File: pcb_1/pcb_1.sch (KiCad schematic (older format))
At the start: 46 parts, among them J1 ACin, J2 Vout, J3 2N3055_conn, J4 DCin, P1 CONN_01X07, P2 CONN_01X01, P3 CONN_01X01, P4 CONN_01X01, P5 CONN_01X01, P6 CONN_01X01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

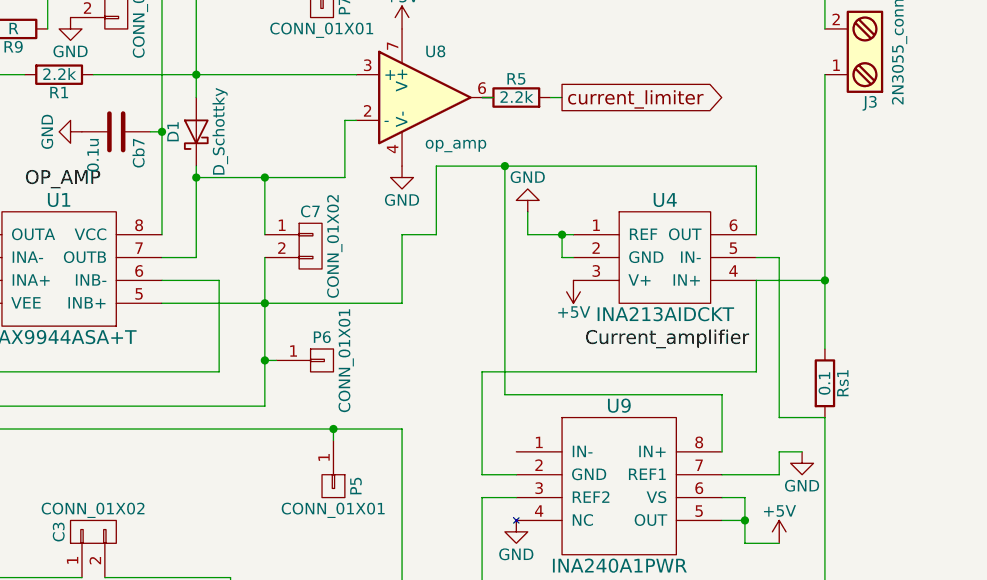
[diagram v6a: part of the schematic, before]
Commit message: INA240 kotelo vaihdettu ja toinen vastaava vahvistin poistettu
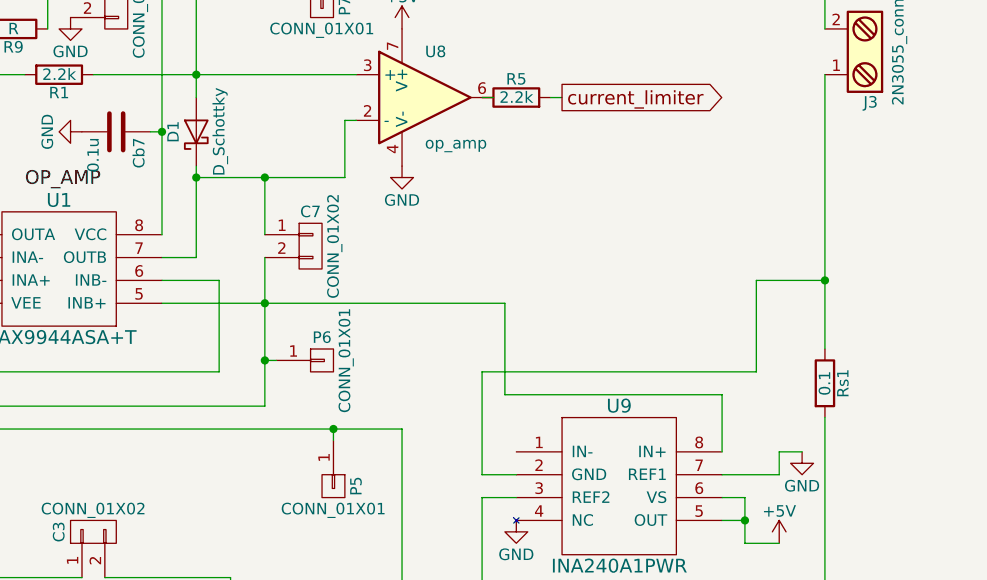
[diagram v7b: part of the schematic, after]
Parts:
- removed U4: INA213AIDCKT, TO_SOT_Packages_SMD:SOT-363_SC-70-6_Handsoldering, symbol INA213AIDCKT
- U9: footprint Housings_SSOP:TSSOP-8_4.4x3mm_Pitch0.65mm -> Housings_SOIC:SOIC-8_3.9x4.9mm_Pitch1.27mm
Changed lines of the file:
@@
-$EndComp
-$Comp
-L INA213AIDCKT U4
-U 1 1 5DA96BAA
-P 9750 2600
-F 0 "U4" H 9750 2850 60  0000 C CNN
-F 1 "INA213AIDCKT" H 9750 2350 60  0000 C CNN
-F 2 "TO_SOT_Packages_SMD:SOT-363_SC-70-6_Handsoldering" H 9750 2550 60  0001 C CNN
-F 3 "" H 9750 2550 60  0001 C CNN
-	1    9750 2600
-	1    0    0    -1
 $EndComp
 $Comp
@@
 $Comp
 L GND #PWR05
-U 1 1 5DA99EAF
-P 9150 2400
-F 0 "#PWR05" H 9150 2150 50  0001 C CNN
-F 1 "GND" H 9150 2250 50  0000 C CNN
-F 2 "" H 9150 2400 50  0000 C CNN
-F 3 "" H 9150 2400 50  0000 C CNN
-	1    9150 2400
-	-1   0    0    1
-$EndComp
-$Comp
-L GND #PWR06
 U 1 1 5DA99EE1
 P 9400 5750
-F 0 "#PWR06" H 9400 5500 50  0001 C CNN
+F 0 "#PWR05" H 9400 5500 50  0001 C CNN
 F 1 "GND" H 9400 5600 50  0000 C CNN
 F 2 "" H 9400 5750 50  0000 C CNN
@@
 $EndComp
 $Comp
-L GND #PWR07
+L GND #PWR06
 U 1 1 5DA99F13
 P 5100 3700
-F 0 "#PWR07" H 5100 3450 50  0001 C CNN
+F 0 "#PWR06" H 5100 3450 50  0001 C CNN
 F 1 "GND" H 5100 3550 50  0000 C CNN
 F 2 "" H 5100 3700 50  0000 C CNN
@@
 $EndComp
 $Comp
-L GND #PWR08
+L GND #PWR07
 U 1 1 5DA99F45
 P 7850 5100
-F 0 "#PWR08" H 7850 4850 50  0001 C CNN
+F 0 "#PWR07" H 7850 4850 50  0001 C CNN
 F 1 "GND" H 7850 4950 50  0000 C CNN
 F 2 "" H 7850 5100 50  0000 C CNN
@@
 $EndComp
 $Comp
-L GND #PWR09
+L GND #PWR08
 U 1 1 5DA9A00F
 P 5900 2200
-F 0 "#PWR09" H 5900 1950 50  0001 C CNN
+F 0 "#PWR08" H 5900 1950 50  0001 C CNN
 F 1 "GND" H 5900 2050 50  0000 C CNN
 F 2 "" H 5900 2200 50  0000 C CNN
@@
 $EndComp
 $Comp
-L GND #PWR010
+L GND #PWR09
 U 1 1 5DA9A041
 P 4400 4250
-F 0 "#PWR010" H 4400 4000 50  0001 C CNN
+F 0 "#PWR09" H 4400 4000 50  0001 C CNN
 F 1 "GND" H 4400 4100 50  0000 C CNN
 F 2 "" H 4400 4250 50  0000 C CNN
@@
 $EndComp
 $Comp
-L GND #PWR011
+L GND #PWR010
 U 1 1 5DA9A073
 P 4400 4650
-F 0 "#PWR011" H 4400 4400 50  0001 C CNN
+F 0 "#PWR010" H 4400 4400 50  0001 C CNN
 F 1 "GND" H 4400 4500 50  0000 C CNN
 F 2 "" H 4400 4650 50  0000 C CNN
@@
 $EndComp
 $Comp
-L GND #PWR012
+L GND #PWR011
 U 1 1 5DA9A83E
 P 6400 4550
-F 0 "#PWR012" H 6400 4300 50  0001 C CNN
+F 0 "#PWR011" H 6400 4300 50  0001 C CNN
 F 1 "GND" H 6400 4400 50  0000 C CNN
 F 2 "" H 6400 4550 50  0000 C CNN
@@
 $EndComp
 $Comp
-L +5V #PWR013
+L +5V #PWR012
 U 1 1 5DA9AC10
 P 6800 4850
-F 0 "#PWR013" H 6800 4700 50  0001 C CNN
+F 0 "#PWR012" H 6800 4700 50  0001 C CNN
 F 1 "+5V" H 6800 4990 50  0000 C CNN
 F 2 "" H 6800 4850 50  0000 C CNN
@@
 Text Label 6950 2300 0    60   ~ 0
 OP_AMP
-Text Label 9400 3000 0    60   ~ 0
-Current_amplifier
 Text Label 7000 5200 0    60   ~ 0
 Charge_pump
@@
 ADC_sda
 $Comp
-L GND #PWR014
+L GND #PWR013
 U 1 1 5DA9DC7C
 P 4550 1300
-F 0 "#PWR014" H 4550 1050 50  0001 C CNN
+F 0 "#PWR013" H 4550 1050 50  0001 C CNN
 F 1 "GND" H 4550 1150 50  0000 C CNN
 F 2 "" H 4550 1300 50  0000 C CNN
@@
 $EndComp
 $Comp
-L GND #PWR015
+L GND #PWR014
 U 1 1 5DA9E862
 P 6450 1600
-F 0 "#PWR015" H 6450 1350 50  0001 C CNN
+F 0 "#PWR014" H 6450 1350 50  0001 C CNN
 F 1 "GND" H 6450 1450 50  0000 C CNN
 F 2 "" H 6450 1600 50  0000 C CNN
@@
 ADC_sda
 $Comp
-L GND #PWR016
+L GND #PWR015
 U 1 1 5DAA07BA
 P 1700 2600
-F 0 "#PWR016" H 1700 2350 50  0001 C CNN
+F 0 "#PWR015" H 1700 2350 50  0001 C CNN
 F 1 "GND" H 1700 2450 50  0000 C CNN
 F 2 "" H 1700 2600 50  0000 C CNN
@@
 $EndComp
 $Comp
-L +5V #PWR017
+L +5V #PWR016
 U 1 1 5DAA1D85
 P 8600 1600
-F 0 "#PWR017" H 8600 1450 50  0001 C CNN
+F 0 "#PWR016" H 8600 1450 50  0001 C CNN
 F 1 "+5V" H 8600 1740 50  0000 C CNN
 F 2 "" H 8600 1600 50  0000 C CNN
@@
 $EndComp
 $Comp
-L GND #PWR018
+L GND #PWR017
 U 1 1 5DAA1DC9
 P 8600 2200
-F 0 "#PWR018" H 8600 1950 50  0001 C CNN
+F 0 "#PWR017" H 8600 1950 50  0001 C CNN
 F 1 "GND" H 8600 2050 50  0000 C CNN
 F 2 "" H 8600 2200 50  0000 C CNN
@@
 $EndComp
 $Comp
-L GND #PWR019
+L GND #PWR018
 U 1 1 5DAA4E05
 P 3200 1200
-F 0 "#PWR019" H 3200 950 50  0001 C CNN
+F 0 "#PWR018" H 3200 950 50  0001 C CNN
 F 1 "GND" H 3200 1050 50  0000 C CNN
 F 2 "" H 3200 1200 50  0000 C CNN
@@
 $EndComp
 $Comp
-L GND #PWR020
+L GND #PWR019
 U 1 1 5DAA97B0
 P 8350 4550
-F 0 "#PWR020" H 8350 4300 50  0001 C CNN
+F 0 "#PWR019" H 8350 4300 50  0001 C CNN
 F 1 "GND" H 8350 4400 50  0000 C CNN
 F 2 "" H 8350 4550 50  0000 C CNN
@@
 $EndComp
 $Comp
-L GND #PWR021
+L GND #PWR020
 U 1 1 5DAAA1EB
 P 6150 2200
-F 0 "#PWR021" H 6150 1950 50  0001 C CNN
+F 0 "#PWR020" H 6150 1950 50  0001 C CNN
 F 1 "GND" H 6150 2050 50  0000 C CNN
 F 2 "" H 6150 2200 50  0000 C CNN
@@
 $EndComp
 $Comp
-L GND #PWR022
+L GND #PWR021
 U 1 1 5DAAA2C9
 P 7150 1550
-F 0 "#PWR022" H 7150 1300 50  0001 C CNN
+F 0 "#PWR021" H 7150 1300 50  0001 C CNN
 F 1 "GND" H 7150 1400 50  0000 C CNN
 F 2 "" H 7150 1550 50  0000 C CNN
@@
 $EndComp
 $Comp
-L GND #PWR023
+L GND #PWR022
 U 1 1 5DAAC6FE
 P 3700 3150
-F 0 "#PWR023" H 3700 2900 50  0001 C CNN
+F 0 "#PWR022" H 3700 2900 50  0001 C CNN
 F 1 "GND" H 3700 3000 50  0000 C CNN
 F 2 "" H 3700 3150 50  0000 C CNN
@@
 $EndComp
 $Comp
-L GND #PWR024
+L GND #PWR023
 U 1 1 5DAAC74C
 P 3200 3000
-F 0 "#PWR024" H 3200 2750 50  0001 C CNN
+F 0 "#PWR023" H 3200 2750 50  0001 C CNN
 F 1 "GND" H 3200 2850 50  0000 C CNN
 F 2 "" H 3200 3000 50  0000 C CNN
@@
 $EndComp
 $Comp
-L GND #PWR025
+L GND #PWR024
 U 1 1 5DAADEFA
 P 5950 1100
-F 0 "#PWR025" H 5950 850 50  0001 C CNN
+F 0 "#PWR024" H 5950 850 50  0001 C CNN
 F 1 "GND" H 5950 950 50  0000 C CNN
 F 2 "" H 5950 1100 50  0000 C CNN
@@
 	1    5950 1100
 	0    -1   -1   0
-$EndComp
-$Comp
-L +5V #PWR026
-U 1 1 5DAB2129
-P 9350 2700
-F 0 "#PWR026" H 9350 2550 50  0001 C CNN
-F 1 "+5V" H 9350 2840 50  0000 C CNN
-F 2 "" H 9350 2700 50  0000 C CNN
-F 3 "" H 9350 2700 50  0000 C CNN
-	1    9350 2700
-	-1   0    0    1
 $EndComp
 $Comp
@@
 $EndComp
 $Comp
-L GND #PWR027
+L GND #PWR025
 U 1 1 5DAB514F
 P 4800 2450
-F 0 "#PWR027" H 4800 2200 50  0001 C CNN
+F 0 "#PWR025" H 4800 2200 50  0001 C CNN
 F 1 "GND" H 4800 2300 50  0000 C CNN
 F 2 "" H 4800 2450 50  0000 C CNN
@@
 $EndComp
 $Comp
-L GND #PWR028
+L GND #PWR026
 U 1 1 5DAB07B7
 P 7200 2050
-F 0 "#PWR028" H 7200 1800 50  0001 C CNN
+F 0 "#PWR026" H 7200 1800 50  0001 C CNN
 F 1 "GND" H 7200 1900 50  0000 C CNN
 F 2 "" H 7200 2050 50  0000 C CNN
@@
 F 0 "U9" H 9550 3950 60  0000 C CNN
 F 1 "INA240A1PWR" H 9550 3250 60  0000 C CNN
-F 2 "Housings_SSOP:TSSOP-8_4.4x3mm_Pitch0.65mm" H 9550 3250 60  0001 C CNN
+F 2 "Housings_SOIC:SOIC-8_3.9x4.9mm_Pitch1.27mm" H 9550 3250 60  0001 C CNN
 F 3 "" H 9550 3250 60  0001 C CNN
 	1    9550 3600
@@
 $EndComp
 $Comp
-L GND #PWR029
+L GND #PWR027
 U 1 1 5DAB6D92
 P 9100 3750
-F 0 "#PWR029" H 9100 3500 50  0001 C CNN
+F 0 "#PWR027" H 9100 3500 50  0001 C CNN
 F 1 "GND" H 9100 3600 50  0000 C CNN
 F 2 "" H 9100 3750 50  0000 C CNN
@@
 $EndComp
 $Comp
-L GND #PWR030
+L GND #PWR028
 U 1 1 5DAB710F
 P 10350 3450
-F 0 "#PWR030" H 10350 3200 50  0001 C CNN
+F 0 "#PWR028" H 10350 3200 50  0001 C CNN
 F 1 "GND" H 10350 3300 50  0000 C CNN
 F 2 "" H 10350 3450 50  0000 C CNN
@@
 $EndComp
 $Comp
-L +5V #PWR031
+L +5V #PWR029
 U 1 1 5DAB72B5
 P 10250 3850
-F 0 "#PWR031" H 10250 3700 50  0001 C CNN
+F 0 "#PWR029" H 10250 3700 50  0001 C CNN
 F 1 "+5V" H 10250 3990 50  0000 C CNN
 F 2 "" H 10250 3850 50  0000 C CNN
@@
 $EndComp
 $Comp
-L GND #PWR032
+L GND #PWR030
 U 1 1 5DABB706
 P 2200 1300
-F 0 "#PWR032" H 2200 1050 50  0001 C CNN
+F 0 "#PWR030" H 2200 1050 50  0001 C CNN
 F 1 "GND" H 2200 1150 50  0000 C CNN
 F 2 "" H 2200 1300 50  0000 C CNN
@@
 $EndComp
 $Comp
-L GND #PWR033
+L GND #PWR031
 U 1 1 5DABD497
 P 1700 1100
-F 0 "#PWR033" H 1700 850 50  0001 C CNN
+F 0 "#PWR031" H 1700 850 50  0001 C CNN
 F 1 "GND" H 1700 950 50  0000 C CNN
 F 2 "" H 1700 1100 50  0000 C CNN
@@
 	7800 2700 7550 2700
 Wire Wire Line
-	10450 3300 10250 3300
-Wire Wire Line
-	10250 3300 10250 2600
-Wire Wire Line
-	10250 2600 10150 2600
-Wire Wire Line
 	10450 1800 10450 3000
 Wire Wire Line
-	10150 2200 10150 2500
-Wire Wire Line
-	7550 2800 8600 2800
+	7550 2800 9050 2800
 Wire Wire Line
 	5350 900  5350 1250
@@
 Wire Wire Line
 	6300 1850 6150 1850
-Wire Wire Line
-	9150 2500 9350 2500
-Wire Wire Line
-	9150 2500 9150 2400
 Wire Wire Line
 	4650 1950 4800 1950
@@
 	6200 2600 6650 2600
 Connection ~ 9400 4950
-Wire Wire Line
-	9350 2600 9300 2600
-Wire Wire Line
-	9300 2600 9300 2500
-Connection ~ 9300 2500
 Wire Wire Line
 	9400 5350 9400 5750
@@
 Connection ~ 8300 4950
 Wire Wire Line
-	8750 2200 10150 2200
-Wire Wire Line
 	10150 2700 10450 2700
 Connection ~ 10450 2700
@@
 	10000 3200 9050 3200
 Wire Wire Line
-	9050 3200 9050 2200
-Connection ~ 9050 2200
-Wire Wire Line
 	8250 1300 8250 1250
 Connection ~ 8250 1250
@@
 Wire Wire Line
 	8000 2600 8000 3250
-Wire Wire Line
-	8600 2800 8600 2500
-Wire Wire Line
-	8600 2500 8750 2500
 Wire Wire Line
 	6350 2950 6350 2700
@@
 	6750 1600 6750 1500
 Wire Wire Line
-	8750 2500 8750 2200
+	9050 3200 9050 2800
 $EndSCHEMATC

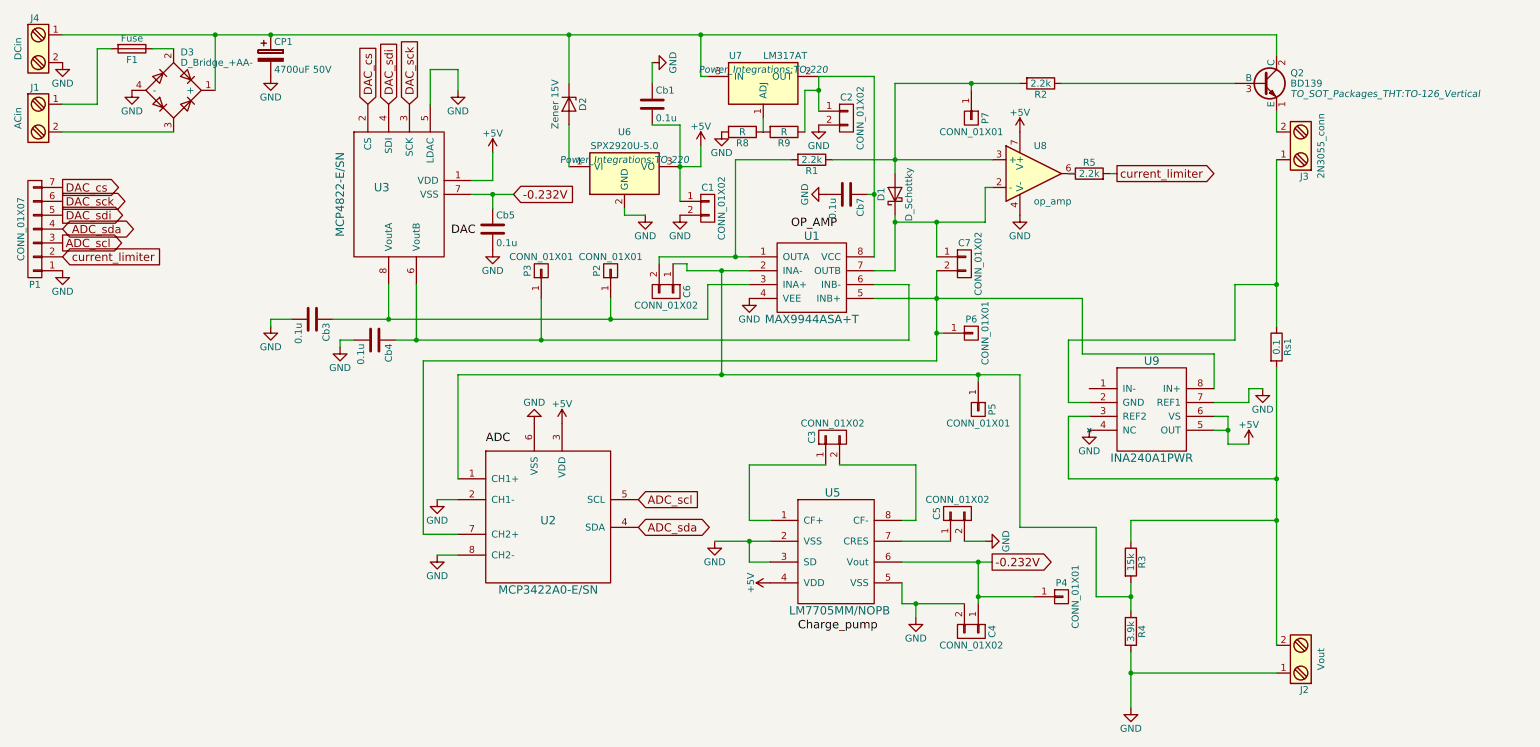
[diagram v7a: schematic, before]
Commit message: pcb:ssa nyt smd- ja tht-komponentit eri puolilla
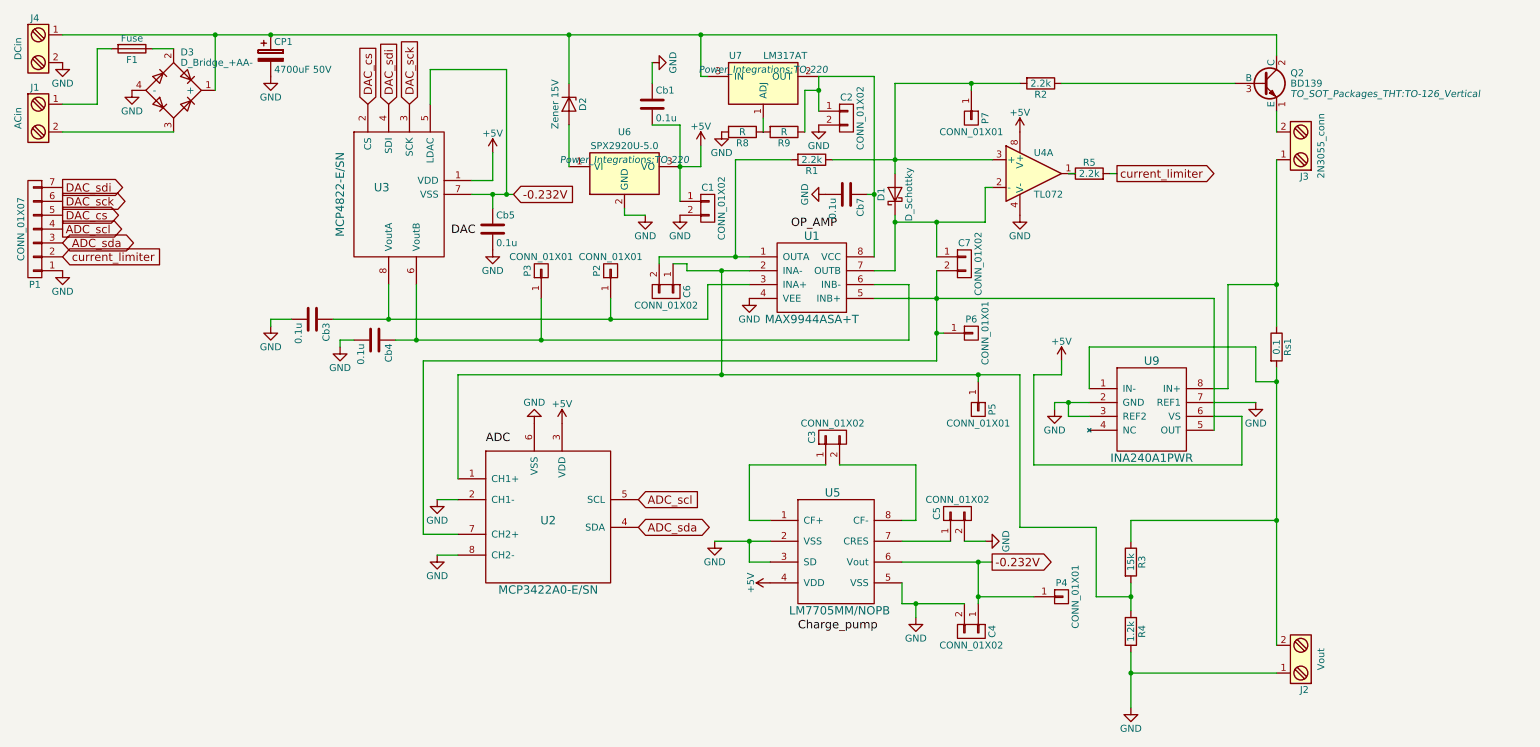
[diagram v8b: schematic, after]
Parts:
- removed U8: op_amp, Housings_SSOP:TSSOP-8_3x3mm_Pitch0.65mm, symbol TL081
- added U4: TL072, Housings_DIP:DIP-8_W7.62mm_Socket_LongPads, symbol OP275
- R1, R2, R3, R5, R8, R9: footprint Resistors_SMD:R_0603_HandSoldering -> Resistors_SMD:R_0805_HandSoldering
- R4: value 3.9k -> 1.2k; footprint Resistors_SMD:R_0603_HandSoldering -> Resistors_SMD:R_0805_HandSoldering
- U1, U2, U3: footprint Housings_SSOP:MSOP-8_3x3mm_Pitch0.65mm -> Housings_SOIC:SOIC-8_3.9x4.9mm_Pitch1.27mm
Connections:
- net +5V: now also U4.8 (V+); no longer U9.5 (OUT)
- net -0.232V: now also U3.5 (LDAC)
- net ADC_scl: now also P1.4 (P4); no longer P1.3 (P3)
- net ADC_sda: now also P1.3 (P3); no longer P1.4 (P4)
- net DAC_cs: now also P1.5 (P5); no longer P1.7 (P7)
- net DAC_sdi: now also P1.7 (P7); no longer P1.5 (P5)
- net GND: now also U9.2 (GND), U9.3 (REF2), U4.4 (V-); no longer U3.5 (LDAC), U9.4 (NC)
- net at C7.2 (P2), P6.1 (P1), U1.5 (INB+)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: now also U9.5 (OUT); no longer U9.8 (IN+)
- net at C7.1 (P1), D1.1 (K), U1.7 (OUTB): now also U4.2 (-)
- net at D1.2 (A), P7.1 (P1), R1.1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: now also U4.3 (+)
- net at J3.1, Rs1.1: now also U9.8 (IN+); no longer U9.2 (GND)
- net at J2.2, R3.1, Rs1.2: now also U9.1 (IN-); no longer U9.3 (REF2)
- net at R5.1: now also U4.1
